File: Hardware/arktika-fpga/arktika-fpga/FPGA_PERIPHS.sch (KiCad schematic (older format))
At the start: 22 parts

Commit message: Assigned some footprints to components
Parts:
- C? (x4): footprint (none) -> Capacitors_SMD:C_0603
- JUSB2: footprint (none) -> Connectors:USB_Micro-B
- R?: footprint (none) -> Resistors_SMD:R_0603
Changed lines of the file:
@@
 F 0 "C?" H 2865 1146 50  0000 L CNN
 F 1 "1u" H 2865 1055 50  0000 L CNN
-F 2 "" H 2788 950 50  0001 C CNN
+F 2 "Capacitors_SMD:C_0603" H 2788 950 50  0001 C CNN
 F 3 "~" H 2750 1100 50  0001 C CNN
 	1    2750 1100
@@
 F 0 "C?" H 2465 1146 50  0000 L CNN
 F 1 "10u" H 2465 1055 50  0000 L CNN
-F 2 "" H 2388 950 50  0001 C CNN
+F 2 "Capacitors_SMD:C_0603" H 2388 950 50  0001 C CNN
 F 3 "~" H 2350 1100 50  0001 C CNN
 	1    2350 1100
@@
 F 0 "C?" H 2865 1796 50  0000 L CNN
 F 1 "1u" H 2865 1705 50  0000 L CNN
-F 2 "" H 2788 1600 50  0001 C CNN
+F 2 "Capacitors_SMD:C_0603" H 2788 1600 50  0001 C CNN
 F 3 "~" H 2750 1750 50  0001 C CNN
 	1    2750 1750
@@
 F 0 "C?" H 2465 1796 50  0000 L CNN
 F 1 "10u" H 2465 1705 50  0000 L CNN
-F 2 "" H 2388 1600 50  0001 C CNN
+F 2 "Capacitors_SMD:C_0603" H 2388 1600 50  0001 C CNN
 F 3 "~" H 2350 1750 50  0001 C CNN
 	1    2350 1750
@@
 F 0 "R?" H 3218 1296 50  0000 L CNN
 F 1 "4.7k" H 3218 1205 50  0000 L CNN
-F 2 "" V 3190 1240 50  0001 C CNN
+F 2 "Resistors_SMD:R_0603" V 3190 1240 50  0001 C CNN
 F 3 "~" H 3150 1250 50  0001 C CNN
 	1    3150 1250
@@
 F 0 "JUSB2" H 1507 2267 50  0000 C CNN
 F 1 "USB_B_Micro" H 1507 2176 50  0000 C CNN
-F 2 "" H 1600 1750 50  0001 C CNN
+F 2 "Connectors:USB_Micro-B" H 1600 1750 50  0001 C CNN
 F 3 "~" H 1600 1750 50  0001 C CNN
 	1    1450 1800

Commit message: Minor fixes
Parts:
- added RN?: R_Pack04, symbol Device:R_Pack04
- added SW?: SW_DIP_x08, symbol Switch:SW_DIP_x08
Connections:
- wire segments 103 -> 131
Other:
- moved on the sheet: D?, RN?, SW?

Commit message: Minor fixes on fpga peripherals
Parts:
- added D?: SP0503BAHT, Package_TO_SOT_SMD:SOT-143, symbol Power_Protection:SP0503BAHT
- added RN? (x2): R_Pack04, symbol Device:R_Pack04
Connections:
- wire segments 131 -> 184
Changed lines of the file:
@@
 	2900 5150 2900 5250
 Entry Bus Bus
-	3500 5050 3600 5150
-Entry Bus Bus
-	3500 5050 3600 5150
-Entry Bus Bus
-	3400 5050 3500 5150
-Entry Bus Bus
-	3300 5050 3400 5150
-Entry Bus Bus
-	3200 5050 3300 5150
-Entry Bus Bus
-	3100 5050 3200 5150
-Entry Bus Bus
-	3000 5050 3100 5150
-Entry Bus Bus
-	2900 5050 3000 5150
-Entry Bus Bus
-	2800 5050 2900 5150
+	3450 5050 3550 5150
+Entry Bus Bus
+	3450 5050 3550 5150
+Entry Bus Bus
+	3350 5050 3450 5150
+Entry Bus Bus
+	3250 5050 3350 5150
+Entry Bus Bus
+	3150 5050 3250 5150
+Entry Bus Bus
+	3050 5050 3150 5150
+Entry Bus Bus
+	2950 5050 3050 5150
+Entry Bus Bus
+	2850 5050 2950 5150
+Entry Bus Bus
+	2750 5050 2850 5150
 Wire Wire Line
 	3250 5850 3300 5850
@@
 	0    -1   -1   0
 $EndComp
+Wire Wire Line
+	2100 2700 2100 2750
+$Comp
+L power:GND #PWR?
+U 1 1 5F21FDC0
+P 2100 2750
+AR Path="/5F21FDC0" Ref="#PWR?"  Part="1"
+AR Path="/5F3E98C5/5F21FDC0" Ref="#PWR?"  Part="1"
+F 0 "#PWR?" H 2100 2500 50  0001 C CNN
+F 1 "GND" H 2100 2600 50  0000 C CNN
+F 2 "" H 2100 2750 50  0001 C CNN
+F 3 "" H 2100 2750 50  0001 C CNN
+	1    2100 2750
+	1    0    0    -1
+$EndComp
+Wire Wire Line
+	2000 2250 2000 2300
+Wire Wire Line
+	2100 2250 2100 2300
+Wire Wire Line
+	2200 2250 2200 2300
+Text Label 2200 2250 1    50   ~ 0
+D-
+Text Label 2100 2250 1    50   ~ 0
+D+
+Text Label 2000 2250 1    50   ~ 0
+Vbus
+$Comp
+L Power_Protection:SP0503BAHT D?
+U 1 1 5F21FDCC
+P 2100 2500
+AR Path="/5F21FDCC" Ref="D?"  Part="1"
+AR Path="/5F3E98C5/5F21FDCC" Ref="D?"  Part="1"
+F 0 "D?" H 2305 2546 50  0000 L CNN
+F 1 "SP0503BAHT" H 2305 2455 50  0000 L CNN
+F 2 "Package_TO_SOT_SMD:SOT-143" H 2325 2450 50  0001 L CNN
+F 3 "http://www.littelfuse.com/~/media/files/littelfuse/technical%20resources/documents/data%20sheets/sp05xxba.pdf" H 2225 2625 50  0001 C CNN
+	1    2100 2500
+	1    0    0    -1
+$EndComp
+Wire Wire Line
+	2850 5150 2900 5150
+Wire Wire Line
+	2950 5150 3000 5150
+Wire Wire Line
+	3050 5150 3100 5150
+Wire Wire Line
+	3150 5150 3200 5150
+Wire Wire Line
+	3250 5150 3300 5150
+Wire Wire Line
+	3350 5150 3400 5150
+Wire Wire Line
+	3450 5150 3500 5150
+Wire Wire Line
+	3550 5150 3600 5150
+$Comp
+L Device:R_Pack04 RN?
+U 1 1 5F256182
+P 3050 4700
+F 0 "RN?" H 2650 4750 50  0000 L CNN
+F 1 "R_Pack04" H 2400 4650 50  0000 L CNN
+F 2 "" V 3325 4700 50  0001 C CNN
+F 3 "~" H 3050 4700 50  0001 C CNN
+	1    3050 4700
+	1    0    0    -1
+$EndComp
+$Comp
+L Device:R_Pack04 RN?
+U 1 1 5F257989
+P 3550 4700
+F 0 "RN?" H 3738 4746 50  0000 L CNN
+F 1 "R_Pack04" H 3738 4655 50  0000 L CNN
+F 2 "" V 3825 4700 50  0001 C CNN
+F 3 "~" H 3550 4700 50  0001 C CNN
+	1    3550 4700
+	1    0    0    -1
+$EndComp
+Wire Wire Line
+	2900 5150 2900 4950
+Wire Wire Line
+	2900 4950 2850 4950
+Wire Wire Line
+	2850 4950 2850 4900
+Connection ~ 2900 5150
+Wire Wire Line
+	3000 5150 3000 4950
+Wire Wire Line
+	3000 4950 2950 4950
+Wire Wire Line
+	2950 4950 2950 4900
+Connection ~ 3000 5150
+Wire Wire Line
+	3100 5150 3100 4950
+Wire Wire Line
+	3100 4950 3050 4950
+Wire Wire Line
+	3050 4950 3050 4900
+Connection ~ 3100 5150
+Wire Wire Line
+	3200 5150 3200 4950
+Wire Wire Line
+	3200 4950 3150 4950
+Wire Wire Line
+	3150 4950 3150 4900
+Connection ~ 3200 5150
+Wire Wire Line
+	3300 5150 3300 4950
+Wire Wire Line
+	3300 4950 3350 4950
+Wire Wire Line
+	3350 4950 3350 4900
+Connection ~ 3300 5150
+Wire Wire Line
+	3400 5150 3400 4950
+Wire Wire Line
+	3400 4950 3450 4950
+Wire Wire Line
+	3450 4950 3450 4900
+Connection ~ 3400 5150
+Wire Wire Line
+	3500 5150 3500 4950
+Wire Wire Line
+	3500 4950 3550 4950
+Wire Wire Line
+	3550 4950 3550 4900
+Connection ~ 3500 5150
+Wire Wire Line
+	3600 5150 3600 4950
+Wire Wire Line
+	3600 4950 3650 4950
+Wire Wire Line
+	3650 4950 3650 4900
+Connection ~ 3600 5150
+Wire Wire Line
+	3650 4500 3650 4450
+Wire Wire Line
+	3650 4450 3550 4450
+Wire Wire Line
+	2850 4450 2850 4500
+Wire Wire Line
+	2950 4450 2950 4500
+Connection ~ 2950 4450
+Wire Wire Line
+	2950 4450 2850 4450
+Wire Wire Line
+	3050 4450 3050 4500
+Connection ~ 3050 4450
+Wire Wire Line
+	3050 4450 2950 4450
+Wire Wire Line
+	3150 4450 3150 4500
+Connection ~ 3150 4450
+Wire Wire Line
+	3150 4450 3050 4450
+Wire Wire Line
+	3350 4450 3350 4500
+Connection ~ 3350 4450
+Wire Wire Line
+	3350 4450 3250 4450
+Wire Wire Line
+	3450 4450 3450 4500
+Connection ~ 3450 4450
+Wire Wire Line
+	3450 4450 3350 4450
+Wire Wire Line
+	3550 4450 3550 4500
+Connection ~ 3550 4450
+Wire Wire Line
+	3550 4450 3450 4450
+Wire Wire Line
+	3250 4350 3250 4450
 Wire Bus Line
 	750  5150 2000 5150
 Wire Bus Line
-	2650 5050 3500 5050
+	2600 5050 3450 5050
 Wire Bus Line
 	4550 4950 6350 4950
+Connection ~ 3250 4450
+Wire Wire Line
+	3250 4450 3150 4450
+Text Label 3250 4350 1    50   ~ 0
+3V3
 $EndSCHEMATC

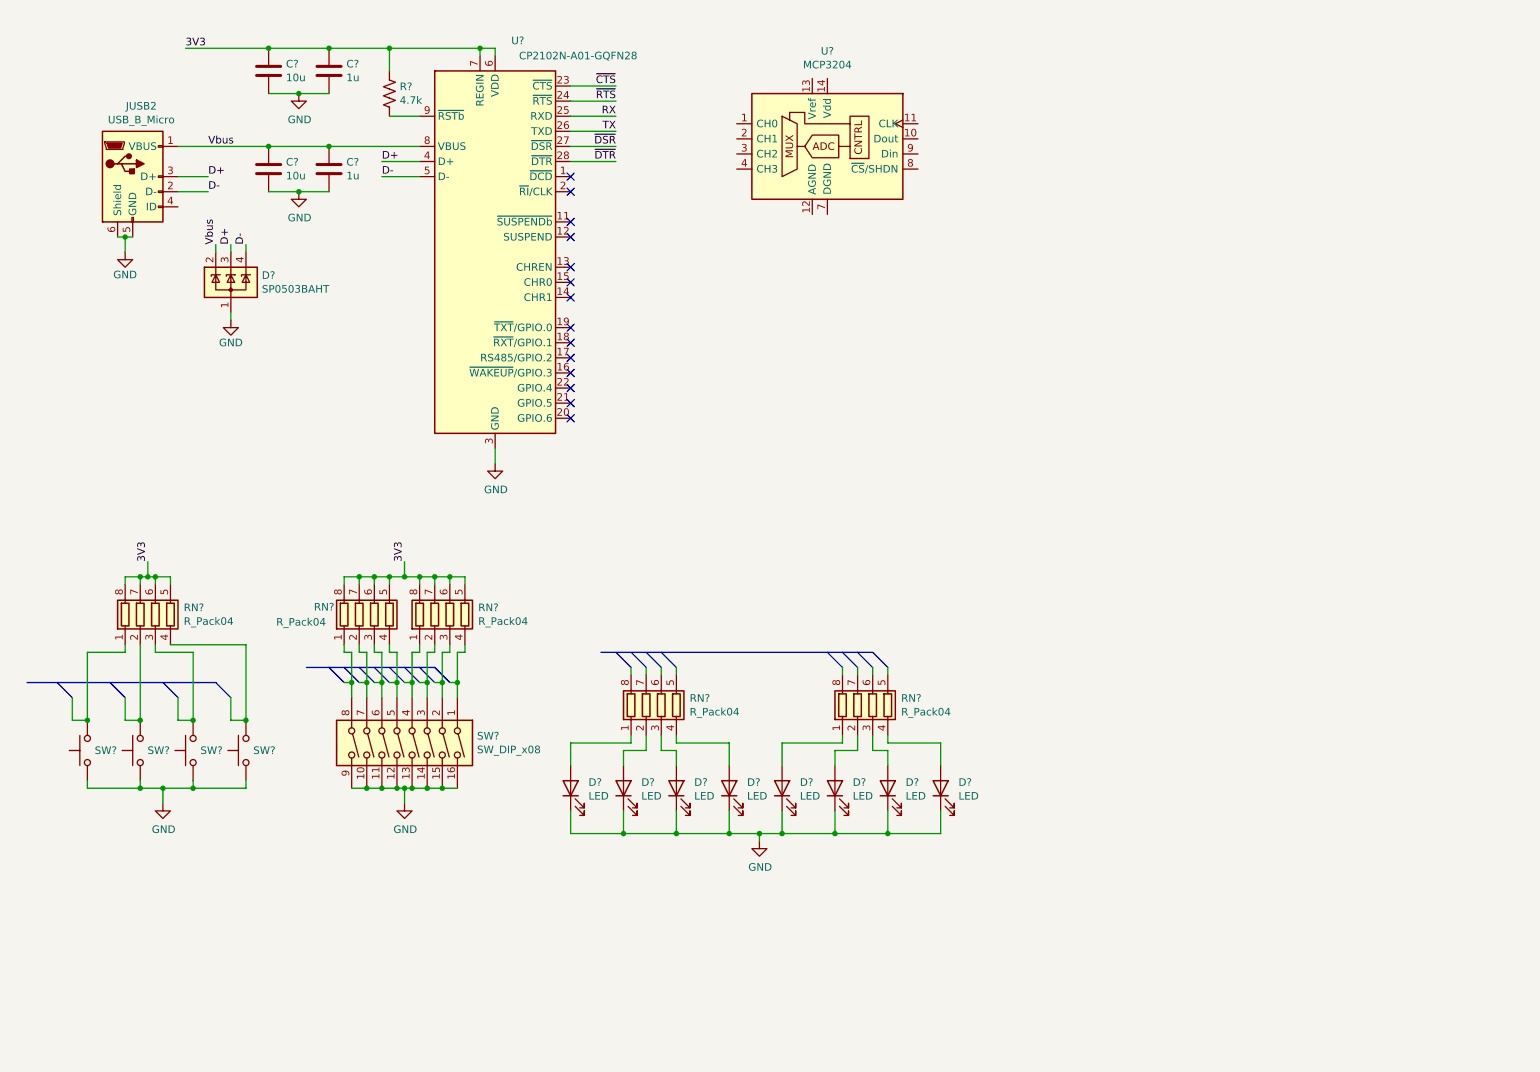
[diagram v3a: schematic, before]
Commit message: Minor fixes, added peripheral buses, added annotations and added crystal datasheets
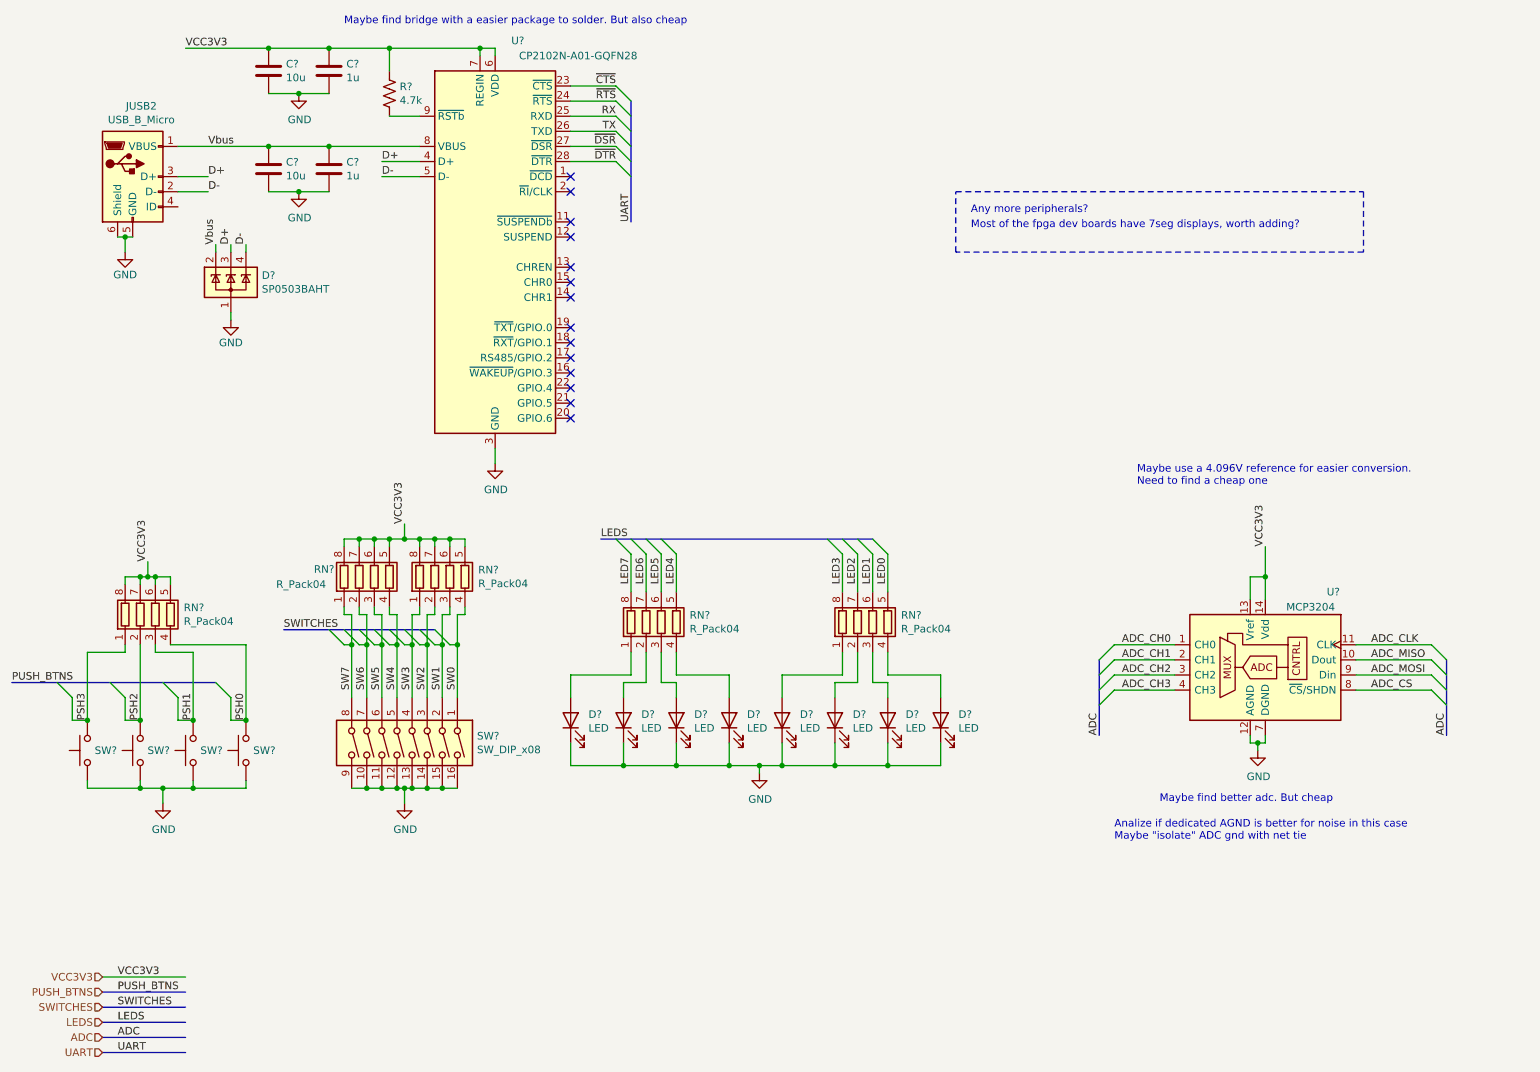
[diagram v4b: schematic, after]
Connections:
- net labels added: ADC, ADC_CH0, ADC_CH1, ADC_CH2, ADC_CH3, ADC_CLK, ADC_CS, ADC_MISO, ADC_MOSI, LED0, LED1, LED2, LED3, LED4, LED5, LED6, LED7, LEDS, PSH0, PSH1, PSH2, PSH3, PUSH_BTNS, SW0, SW1, SW2, SW3, SW4, SW5, SW6, SW7, SWITCHES, UART, VCC3V3
- net labels removed: 3V3
- wire segments 184 -> 202
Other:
- note added: "Analize if dedicated AGND is better for noise in this case\nMaybe "isolate" ADC gnd with net tie"
- note added: "Any more peripherals?"
- note added: "Maybe find better adc. But cheap\n"
- note added: "Maybe find bridge with a easier package to solder. But also cheap\n"
- note added: "Maybe use a 4.096V reference for easier conversion.\nNeed to find a cheap one"
- note added: "Most of the fpga dev boards have 7seg displays, worth adding?"
- moved on the sheet: D?, RN?, U?

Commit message: Added alternate power intput. Update some designators. Added fpga crystal
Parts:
- RPER2, RPER3, RPER4: renamed from RN?; value R_Pack04 -> 1k
- RPER5, RPER6: renamed from RN?; value R_Pack04 -> 660?
- gave numbers to parts that had none: 20
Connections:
- no-connect marks 14 -> 15
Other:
- moved on the sheet: CPER1, CPER3

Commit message: Added fuse to usb peripheral, other minor changes
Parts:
- added F?: 500mA?, symbol Device:Fuse
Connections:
- net Vbus: now also F?.1; no longer JUSB2.1 (VBUS)
- new net: F?.2, JUSB2.1 (VBUS)
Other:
- moved on the sheet: JUSB2
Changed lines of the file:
@@
 Sheet 5 5
 Title "Arktika FPGA"
-Date "2020-07-29"
+Date "2020-07-30"
 Rev ""
-Comp "Author: Afonso Muralha"
+Comp "Authors: Afonso Muralha and João Nuno Carvalho"
 Comment1 ""
 Comment2 ""
@@
 NoConn ~ 4350 3400
 Wire Wire Line
-	1400 2200 1400 2300
-Wire Wire Line
-	1400 2200 1450 2200
-Connection ~ 1400 2200
-Wire Wire Line
-	1350 2200 1400 2200
+	950  2200 950  2300
+Wire Wire Line
+	950  2200 1000 2200
+Connection ~ 950  2200
+Wire Wire Line
+	900  2200 950  2200
 $Comp
 L power:GND #PWR?
 U 1 1 5F751C99
-P 1400 2300
+P 950 2300
 AR Path="/5F751C99" Ref="#PWR?"  Part="1"
 AR Path="/5F3E98C5/5F751C99" Ref="#PWR?"  Part="1"
 AR Path="/5F72015E/5F751C99" Ref="#PWR?"  Part="1"
-F 0 "#PWR?" H 1400 2050 50  0001 C CNN
-F 1 "GND" H 1400 2150 50  0000 C CNN
-F 2 "" H 1400 2300 50  0001 C CNN
-F 3 "" H 1400 2300 50  0001 C CNN
-	1    1400 2300
-	1    0    0    -1
-$EndComp
-Text Label 1950 1900 0    50   ~ 0
+F 0 "#PWR?" H 950 2050 50  0001 C CNN
+F 1 "GND" H 950 2150 50  0000 C CNN
+F 2 "" H 950 2300 50  0001 C CNN
+F 3 "" H 950 2300 50  0001 C CNN
+	1    950  2300
+	1    0    0    -1
+$EndComp
+Text Label 1500 1900 0    50   ~ 0
 D-
-Text Label 1950 1800 0    50   ~ 0
+Text Label 1500 1800 0    50   ~ 0
 D+
 Text Label 1950 1600 0    50   ~ 0
@@
 L Connector:USB_B_Micro JUSB?
 U 1 1 5F751CA2
-P 1450 1800
+P 1000 1800
 AR Path="/5F751CA2" Ref="JUSB?"  Part="1"
 AR Path="/5F3E98C5/5F751CA2" Ref="JUSB?"  Part="1"
 AR Path="/5F72015E/5F751CA2" Ref="JUSB2"  Part="1"
-F 0 "JUSB2" H 1507 2267 50  0000 C CNN
-F 1 "USB_B_Micro" H 1507 2176 50  0000 C CNN
-F 2 "Connectors:USB_Micro-B" H 1600 1750 50  0001 C CNN
-F 3 "~" H 1600 1750 50  0001 C CNN
-	1    1450 1800
-	1    0    0    -1
-$EndComp
-Wire Wire Line
-	1950 1800 1750 1800
-Wire Wire Line
-	1750 1900 1950 1900
-Wire Wire Line
-	1750 1600 2250 1600
+F 0 "JUSB2" H 1057 2267 50  0000 C CNN
+F 1 "USB_B_Micro" H 1057 2176 50  0000 C CNN
+F 2 "Connectors:USB_Micro-B" H 1150 1750 50  0001 C CNN
+F 3 "~" H 1150 1750 50  0001 C CNN
+	1    1000 1800
+	1    0    0    -1
+$EndComp
+Wire Wire Line
+	1500 1800 1300 1800
+Wire Wire Line
+	1300 1900 1500 1900
 Wire Wire Line
 	2750 950  3150 950
@@
 	0    -1   -1   0
 $EndComp
-NoConn ~ 1750 2000
+NoConn ~ 1300 2000
+$Comp
+L Device:Fuse F?
+U 1 1 5F2413DD
+P 1500 1600
+AR Path="/5F2413DD" Ref="F?"  Part="1"
+AR Path="/5F3E98C5/5F2413DD" Ref="F?"  Part="1"
+AR Path="/5F72015E/5F2413DD" Ref="F?"  Part="1"
+F 0 "F?" V 1303 1600 50  0000 C CNN
+F 1 "500mA?" V 1394 1600 50  0000 C CNN
+F 2 "" V 1430 1600 50  0001 C CNN
+F 3 "~" H 1500 1600 50  0001 C CNN
+	1    1500 1600
+	0    1    1    0
+$EndComp
+Wire Wire Line
+	1300 1600 1350 1600
+Wire Wire Line
+	1650 1600 2250 1600
 Wire Bus Line
 	7850 5000 7850 5500
